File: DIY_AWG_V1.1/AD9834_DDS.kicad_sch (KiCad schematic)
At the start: 67 parts, among them IC1 TLV3544IPWR, IC2 ADG704BRMZ-REEL7, U11 8121H-50.000NK33DRL, U12 AD9834, U13 OPA2171AIDR

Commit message: Updated component footprints
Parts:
- C44: footprint (none) -> Capacitor_SMD:C_0603_1608Metric; Component Name (none) -> TCC0603COG200G500CT; LCSC ID (none) -> C5360848
- C45: footprint (none) -> Capacitor_SMD:C_0603_1608Metric; Component Name (none) -> C0603C470F5GACAUTO; LCSC ID (none) -> C1865294
- R14: footprint (none) -> Capacitor_SMD:C_0603_1608Metric; Component Name (none) -> ARG03BTC2000; LCSC ID (none) -> C37635738
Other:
- moved on the sheet: C44, C45, C48, C51, C52, C54, C57, C60, L10, L7, L8, R21

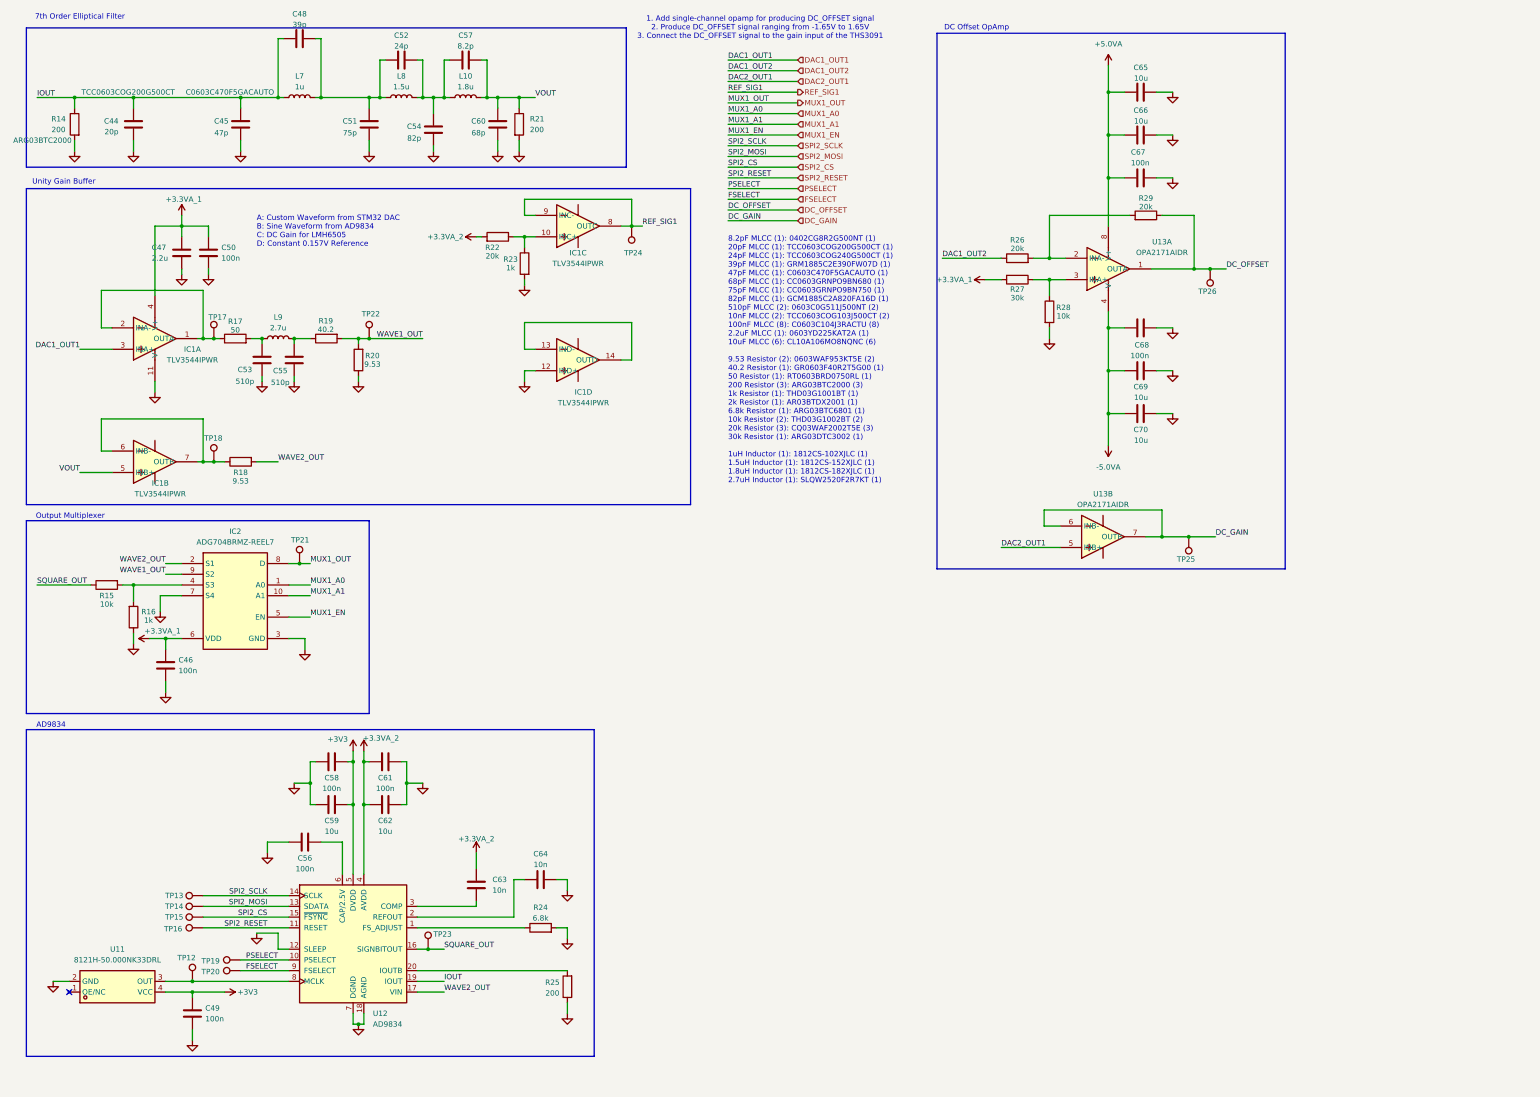
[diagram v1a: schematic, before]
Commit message: Updated component footprints
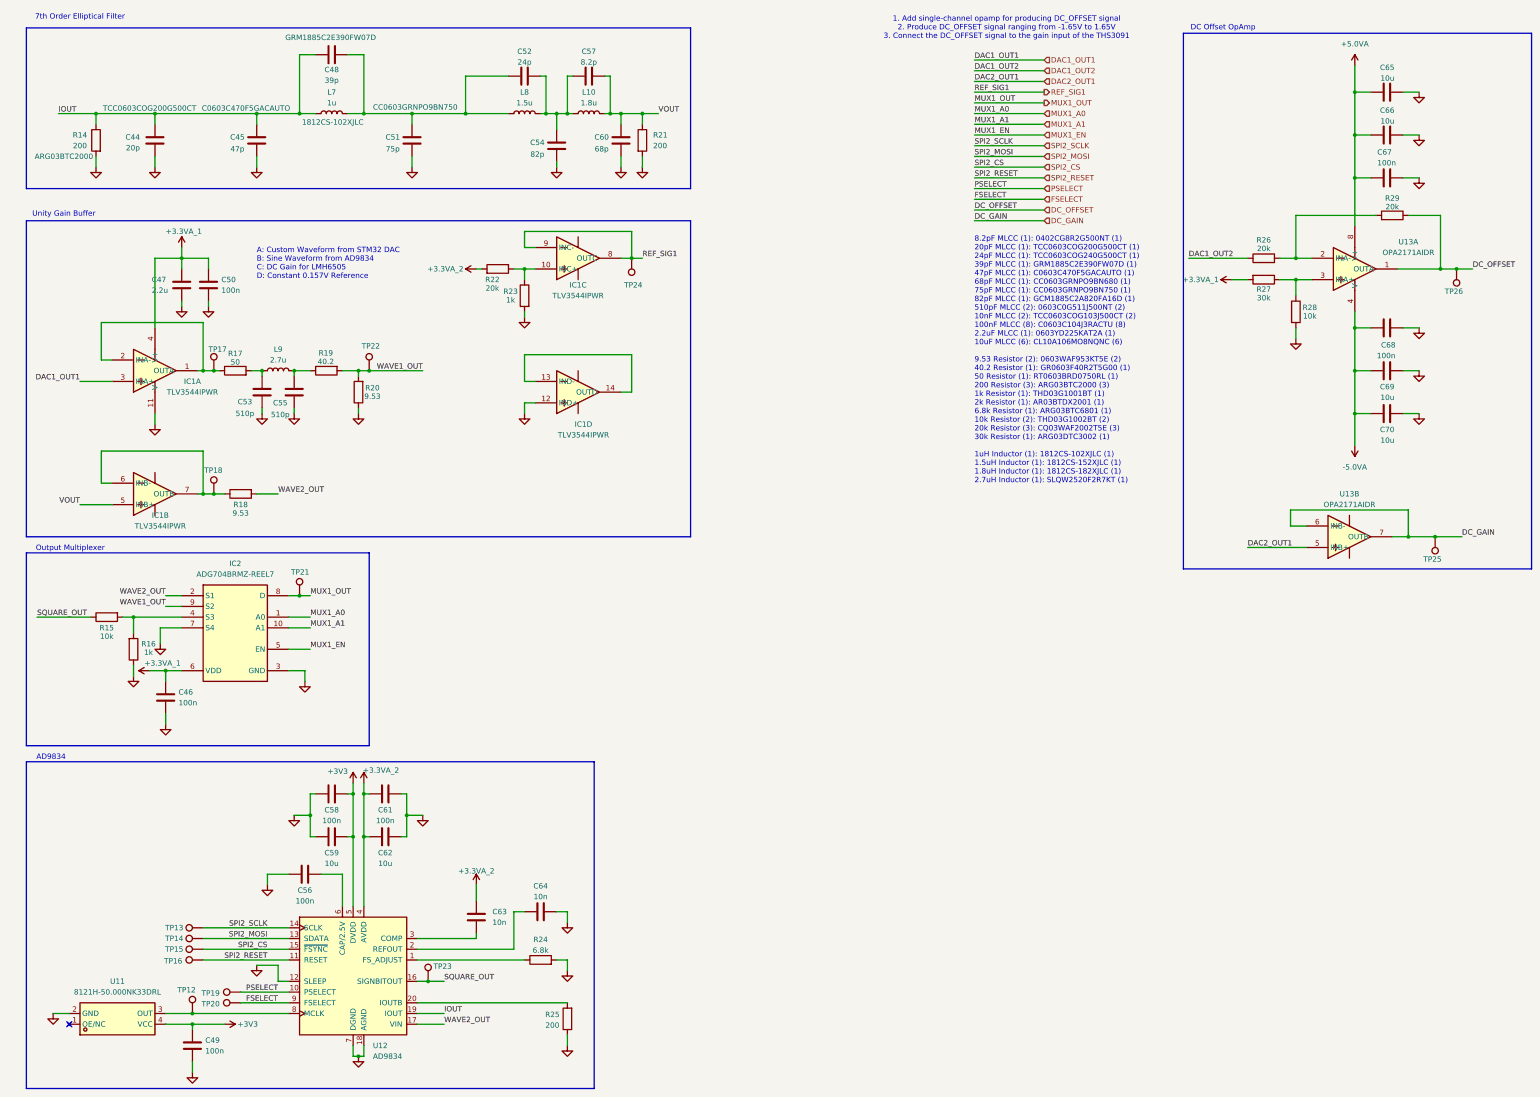
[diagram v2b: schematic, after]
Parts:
- C48: footprint (none) -> Capacitor_SMD:C_0603_1608Metric; Component Name (none) -> GRM1885C2E390FW07D; LCSC ID (none) -> C22124185
- C51: footprint (none) -> Capacitor_SMD:C_0603_1608Metric; Component Name (none) -> CC0603GRNPO9BN750; LCSC ID (none) -> C519466
- L7: footprint (none) -> Inductor_SMD:L_1812_4532Metric; Component Name (none) -> 1812CS-102XJLC; LCSC ID (none) -> C37639398
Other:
- moved on the sheet: C44, C45, C46, C47, C48, C49, C50, C51, C52, C53, C54, C55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

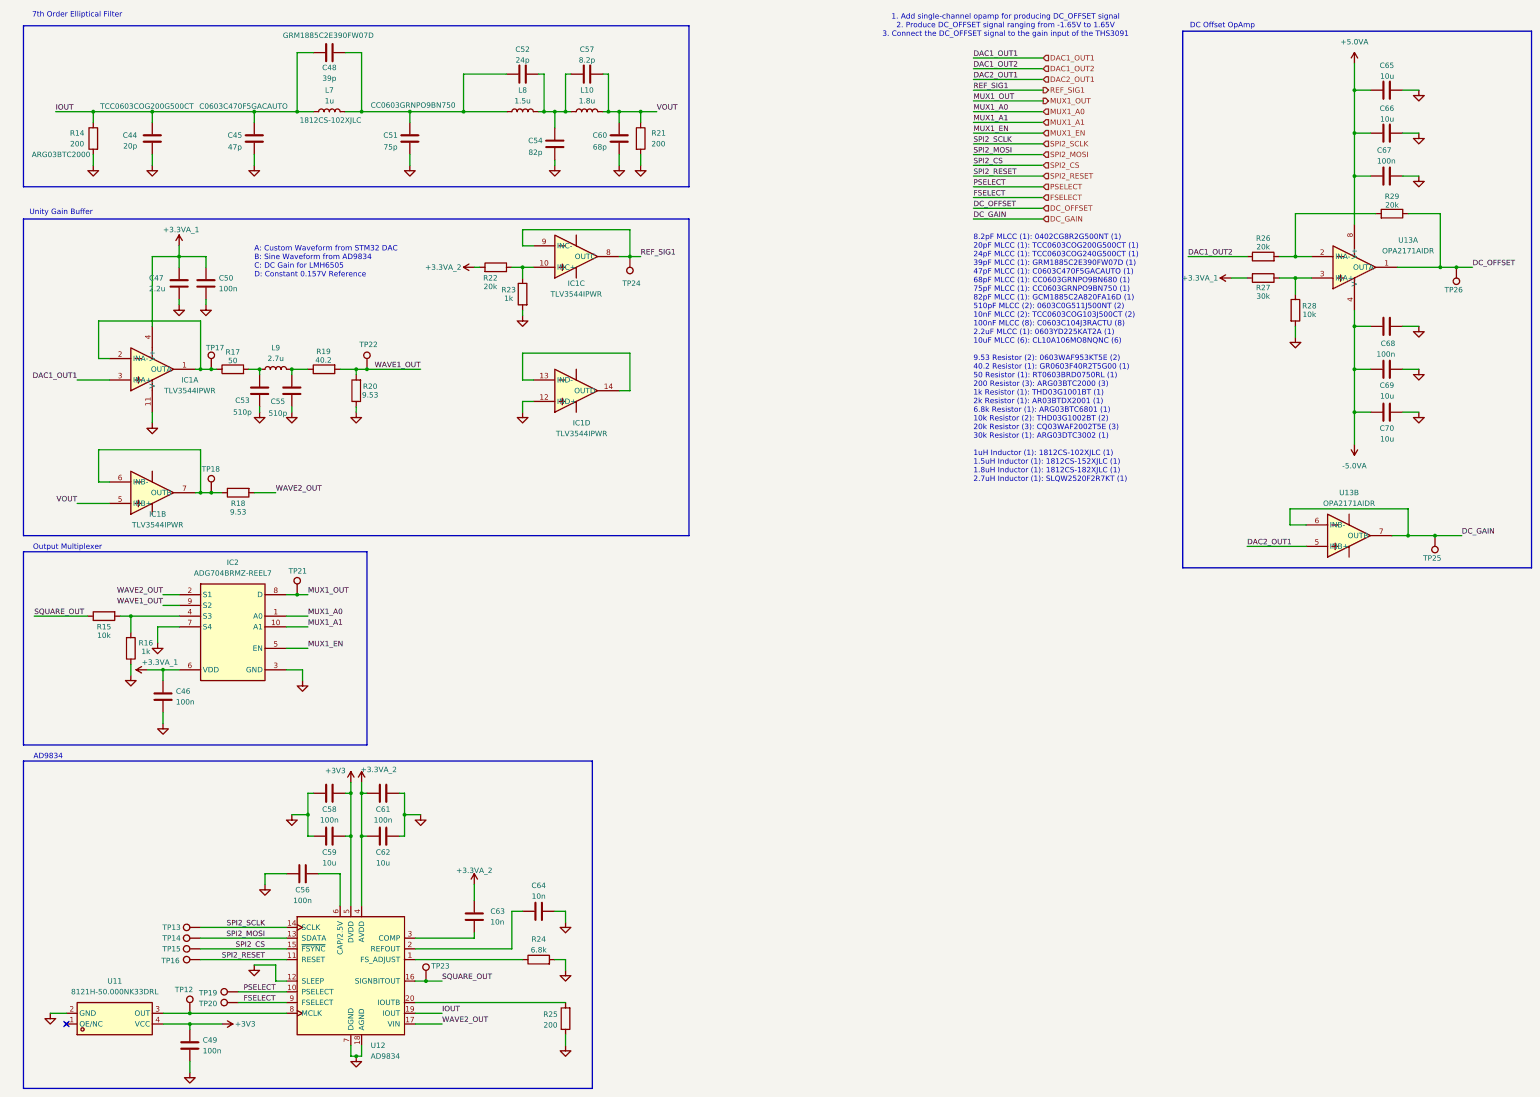
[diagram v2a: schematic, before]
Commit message: Updated component footprints
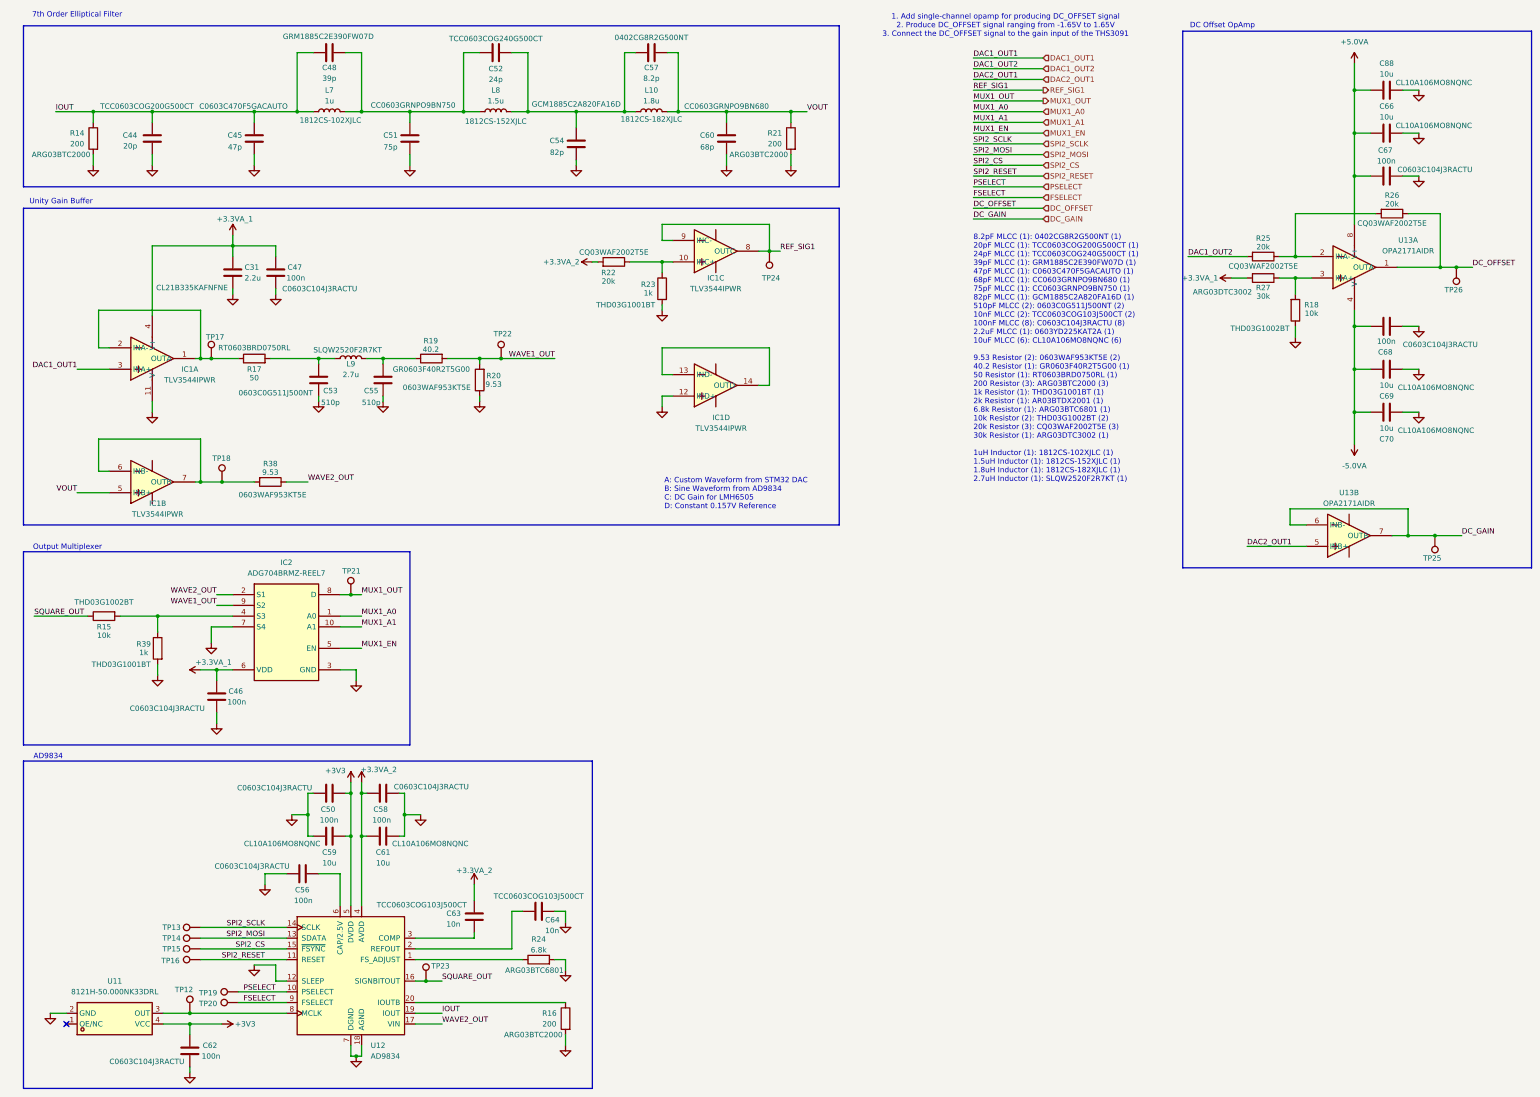
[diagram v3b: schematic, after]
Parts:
- removed C49: 100n, symbol Device:C
- removed C65: 10u, symbol Device:C
- removed R28: 10k, symbol Device:R
- removed R29: 20k, symbol Device:R
- added C31: 2.2u, Capacitor_SMD:C_0805_2012Metric, symbol Device:C
- added C88: 10u, Capacitor_SMD:C_0603_1608Metric, symbol Device:C
- added R38: 9.53, Resistor_SMD:R_0603_1608Metric, symbol Device:R
- added R39: 1k, Resistor_SMD:R_0603_1608Metric, symbol Device:R
- C46, C50, C56, C58, C67, C68: footprint (none) -> Capacitor_SMD:C_0603_1608Metric; Component Name (none) -> C0603C104J3RACTU; LCSC ID (none) -> C2167388
- C47: value 2.2u -> 100n; footprint (none) -> Capacitor_SMD:C_0603_1608Metric; Component Name (none) -> C0603C104J3RACTU; LCSC ID (none) -> C2167388
- C52: footprint (none) -> Capacitor_SMD:C_0603_1608Metric; Component Name (none) -> TCC0603COG240G500CT; LCSC ID (none) -> C5375817
- C53: footprint (none) -> Capacitor_SMD:C_0603_1608Metric; Component Name (none) -> 0603C0G511J500NT; LCSC ID (none) -> C49326333
- C54: footprint (none) -> Capacitor_SMD:C_0603_1608Metric; Component Name (none) -> GCM1885C2A820FA16D; LCSC ID (none) -> C1864236
- C57: footprint (none) -> Capacitor_SMD:C_0402_1005Metric; Component Name (none) -> 0402CG8R2G500NT; LCSC ID (none) -> C2857971
- C59, C66, C69, C70: footprint (none) -> Capacitor_SMD:C_0603_1608Metric; Component Name (none) -> CL10A106MO8NQNC; LCSC ID (none) -> C92487
- C60: footprint (none) -> Capacitor_SMD:C_0603_1608Metric; Component Name (none) -> CC0603GRNPO9BN680; LCSC ID (none) -> C519457
- C61: value 100n -> 10u; footprint (none) -> Capacitor_SMD:C_0603_1608Metric; Component Name (none) -> CL10A106MO8NQNC; LCSC ID (none) -> C92487
- C62: value 10u -> 100n; footprint (none) -> Capacitor_SMD:C_0603_1608Metric; Component Name (none) -> C0603C104J3RACTU; LCSC ID (none) -> C2167388
- C63, C64: footprint (none) -> Capacitor_SMD:C_0603_1608Metric; Component Name (none) -> TCC0603COG103J500CT; LCSC ID (none) -> C7393880
- L10: footprint (none) -> Inductor_SMD:L_1812_4532Metric; Component Name (none) -> 1812CS-182XJLC; LCSC ID (none) -> C38811900
- L8: footprint (none) -> Inductor_SMD:L_1812_4532Metric; Component Name (none) -> 1812CS-152XJLC; LCSC ID (none) -> C39924671
- L9: footprint (none) -> easyeda2kicad:L_SMD_SLQW2520_2.9x2.7; Component Name (none) -> SLQW2520F2R7KT; LCSC ID (none) -> C42440934
- R15: footprint (none) -> Resistor_SMD:R_0603_1608Metric; Component Name (none) -> THD03G1002BT; LCSC ID (none) -> C47120023
- R16: value 1k -> 200; footprint (none) -> Capacitor_SMD:C_0603_1608Metric; Component Name (none) -> ARG03BTC2000; LCSC ID (none) -> C37635738
- R17: footprint (none) -> Resistor_SMD:R_0603_1608Metric; Component Name (none) -> RT0603BRD0750RL; LCSC ID (none) -> C5879483
- R18: value 9.53 -> 10k; footprint (none) -> Resistor_SMD:R_0603_1608Metric; Component Name (none) -> THD03G1002BT; LCSC ID (none) -> C47120023
- R19: footprint (none) -> Resistor_SMD:R_0603_1608Metric; Component Name (none) -> GR0603F40R2T5G00; LCSC ID (none) -> C49654821
- R20: footprint (none) -> Resistor_SMD:R_0603_1608Metric; Component Name (none) -> 0603WAF953KT5E; LCSC ID (none) -> C407502
- R21: footprint (none) -> Capacitor_SMD:C_0603_1608Metric; Component Name (none) -> ARG03BTC2000; LCSC ID (none) -> C37635738
- R22, R26: footprint (none) -> Resistor_SMD:R_0603_1608Metric; Component Name (none) -> CQ03WAF2002T5E; LCSC ID (none) -> C2765619
- R23: footprint (none) -> Resistor_SMD:R_0603_1608Metric; Component Name (none) -> THD03G1001BT; LCSC ID (none) -> C52104281
- R24: footprint (none) -> Capacitor_SMD:C_0603_1608Metric; Component Name (none) -> ARG03BTC6801; LCSC ID (none) -> C2941290
- R25: value 200 -> 20k; footprint (none) -> Resistor_SMD:R_0603_1608Metric; Component Name (none) -> CQ03WAF2002T5E; LCSC ID (none) -> C2765619
- R27: footprint (none) -> Resistor_SMD:R_0603_1608Metric; Component Name (none) -> ARG03DTC3002; LCSC ID (none) -> C2758295
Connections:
- net +3.3VA_1: now also C31.1; no longer C50.1
- net +3.3VA_2: now also C58.2, C61.2; no longer C61.1, C62.1
- net +3V3: now also C50.2, C62.2; no longer C58.2
- net +5.0VA: now also C66.2, C67.2, C88.2; no longer C66.1, C67.1
- net -5.0VA: now also C68.2, C69.2, C70.2; no longer C68.1, C69.1, C70.1
- net DAC1_OUT2: now also R25.2; no longer R26.1
- net DC_OFFSET: now also R26.1
- net GND: now also C50.1, C61.1, C62.1, C64.1, C66.1, C67.1, C68.1, C69.1, C70.1, R16.2, R18.1, C31.2, C88.1, R39.2; no longer C50.2, C61.2, C62.2, C64.2, C66.2, C67.2, C68.2, C69.2, C70.2, R16.1, R25.1
- net WAVE2_OUT: now also R38.1; no longer R18.2
- net at IC1.6 (INB-), IC1.7 (OUTB), TP18.1: now also R38.2; no longer R18.1
- net at U12.2 (REFOUT): now also C64.2; no longer C64.1
- net at U12.20 (IOUTB): now also R16.1; no longer R25.2
- net at R26.2, U13.2 (INA-): now also R25.1
- net at R27.1, U13.3 (INA+): now also R18.2
- net at IC2.4 (S3), R15.2: now also R39.1; no longer R16.2
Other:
- moved on the sheet: C52, C53, C54, C55, C57, C60, IC1A, IC1B, IC1C, IC1D, IC2, L10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
